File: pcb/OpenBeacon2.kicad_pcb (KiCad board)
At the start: 4 copper layers, 120 x 100 mm, 262 parts, among them J1 Bias V, J10 UART, J11 BNC, J12 USB_C_Receptacle, J13 UPDI, J14 PPS, J15 U.FL, J16 SMA CLKIN, J2 PAI+, J3 PAI-, J4 Digital IO, J5 ADC Inputs, J6 SMA, J8 I2C Bus, J9 GND, K1 G6K-2F-Y-DC5, K2 G6K-2F-Y-DC5, K3 G6K-2F-Y-DC5, K4 G6K-2F-Y-DC5, K5 G6K-2F-Y-DC5, K6 G6K-2F-Y-DC5, Q1 2N7002, Q2 MMBT4403, Q3 BS170, Q4 2N7002, Q5 2N7002, Q6 AO3400A, Q7 AO3400A, Q8 BS170, U1 TLV61046A, U10 CP2102N-A02-GQFN24, U11 TLV75533PDBV, U12 MAX-M10S-00B, U13 TPS22941, U2 25.000 MHz TCXO, U3 SN74LVC1G17, U4 SI5351C-B-GMR, U5 MCP4725A1T-E/CH, U8 24AA64T, U9 AVR128DA48-E/PT, Y1 32.768kHz

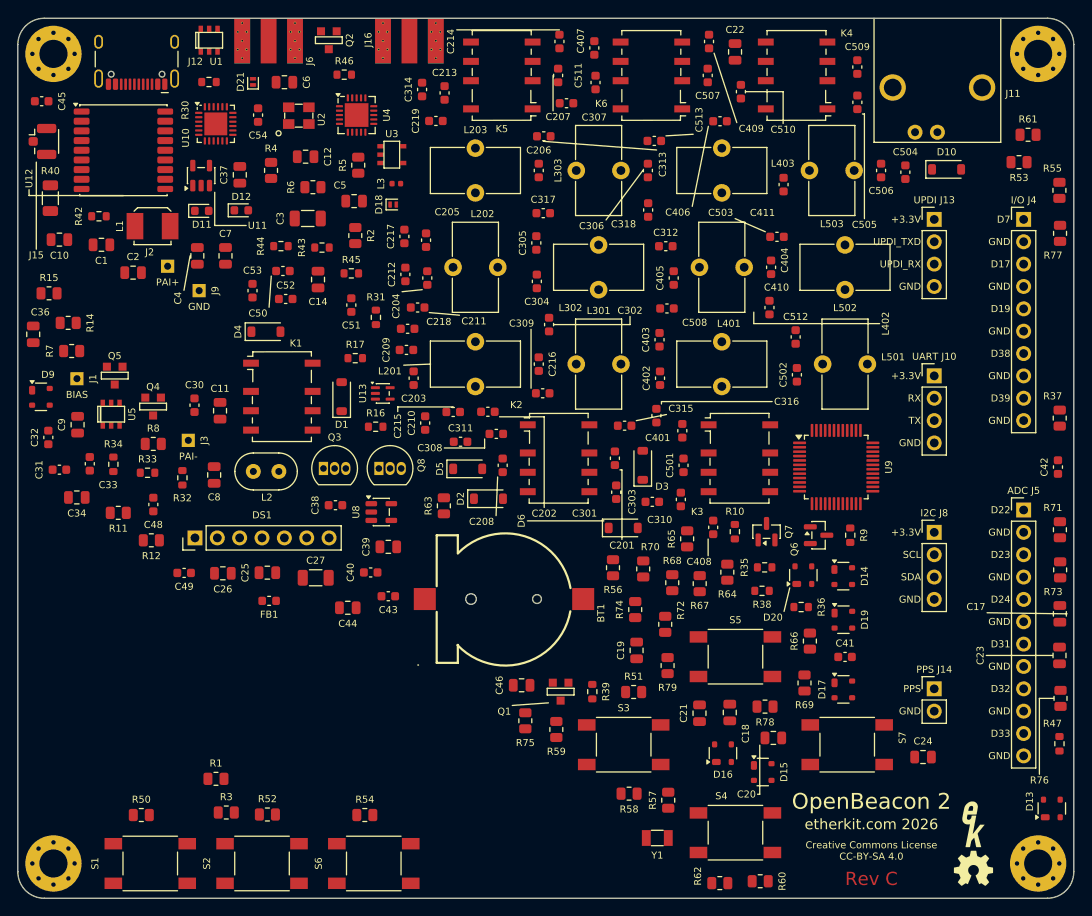
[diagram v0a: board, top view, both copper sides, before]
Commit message: S1-S7: Kinghelm KH-6X6X13H-STM 13 mm (C2837539); K5/K6 clear of case-bulkhead strip; gate check 7
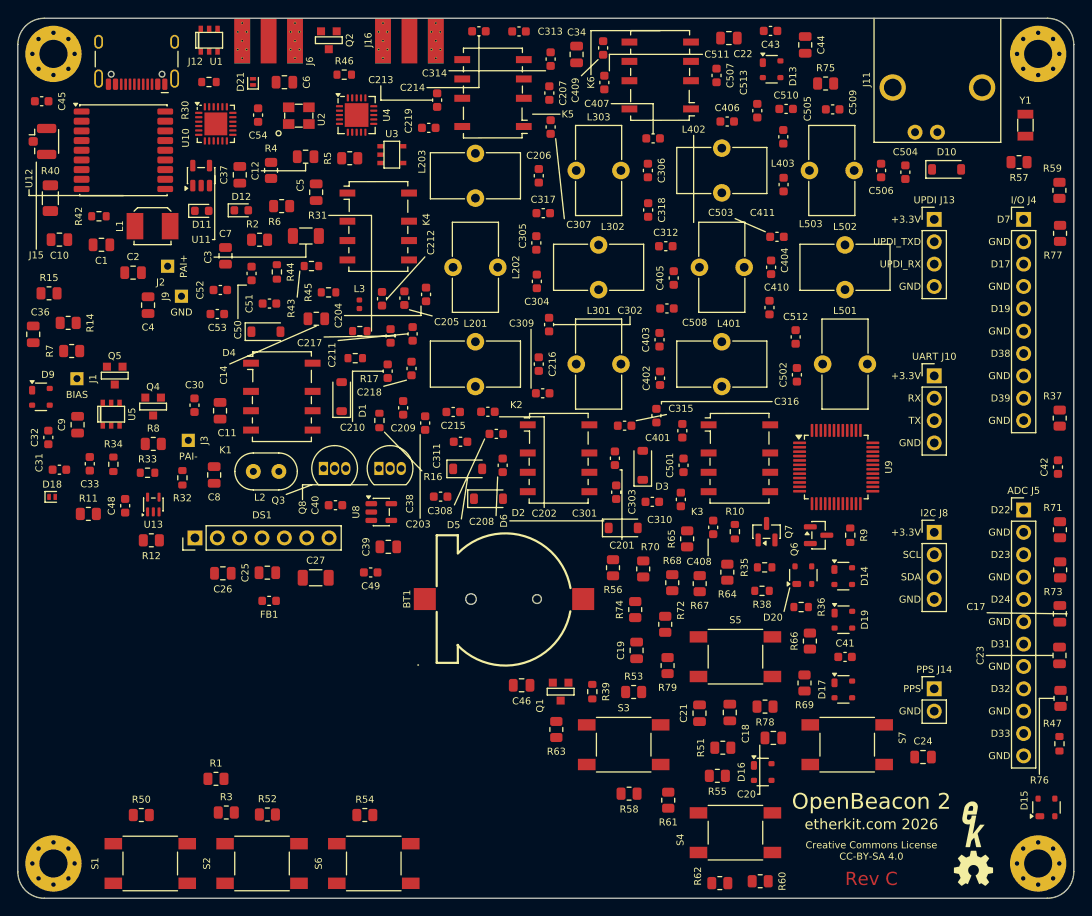
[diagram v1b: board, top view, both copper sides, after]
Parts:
- moved Y1 91.2 mm to (214.5, 112.2), turned to 90 degrees
- moved D13 89.8 mm to (185.7, 105.8), turned to 0 degrees
- moved R61 86.0 mm to (173.9, 188.9), turned to 90 degrees
- moved R59 83.8 mm to (218.4, 119.6)
- moved R57 82.7 mm to (213.8, 116.4), turned to 0 degrees
- moved C44 82.4 mm to (189.5, 103.0), turned to 90 degrees
- moved R75 80.1 mm to (191.8, 107.4), turned to 0 degrees
- moved C43 77.5 mm to (185.5, 101.4)
- moved R55 77.1 mm to (179.5, 186.1), turned to 0 degrees
- moved C34 75.9 mm to (163.5, 104.1), turned to 90 degrees
- moved R53 74.5 mm to (170.0, 176.6)
- moved D18 51.0 mm to (103.9, 154.4)
- moved K4 50.5 mm to (141.0, 123.7), turned to 0 degrees
- moved D15 32.5 mm to (216.9, 189.7), turned to 90 degrees
- moved U13 29.0 mm to (115.4, 155.3), turned to 90 degrees
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
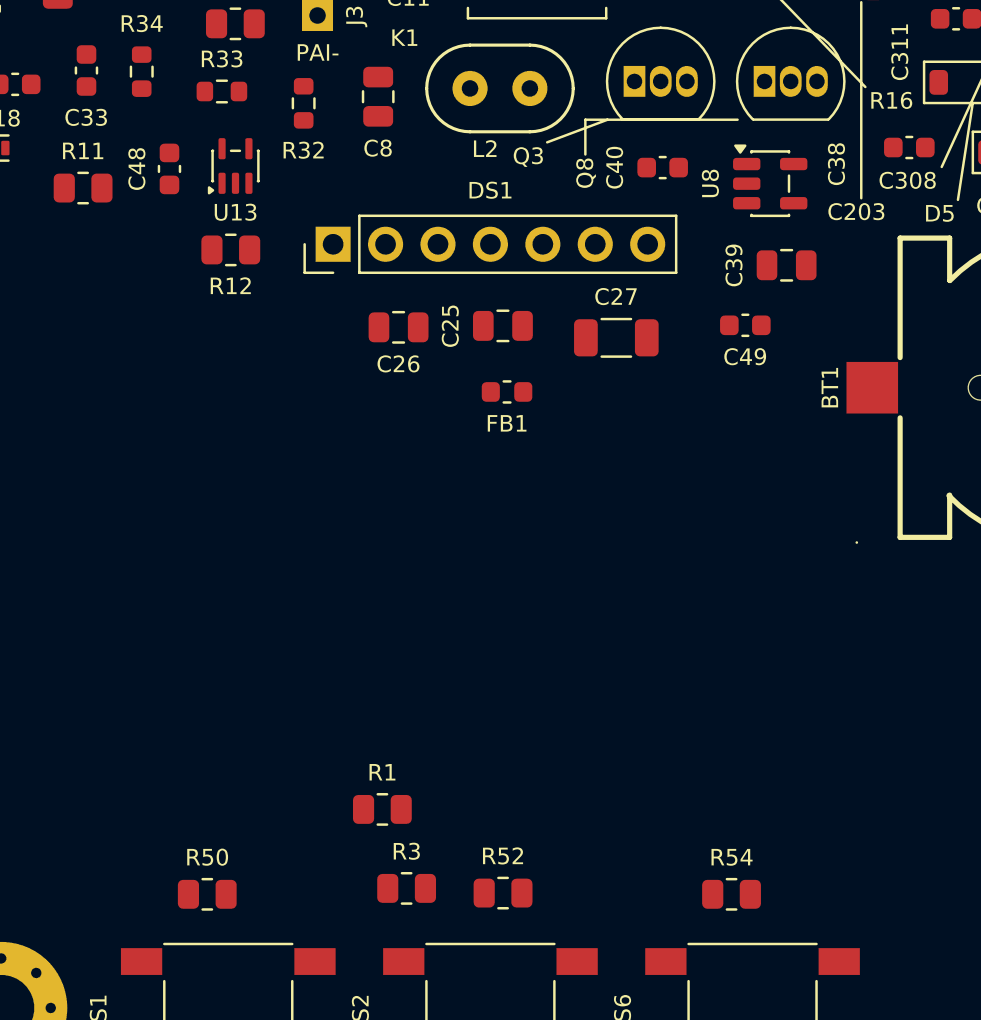
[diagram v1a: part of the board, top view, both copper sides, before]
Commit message: DS1: full 1.3in OLED module outline on F.SilkS (35.4x33.5, VFO style); U8 out from under module; gate check 8 (only low R/C/FB/L under DS1)
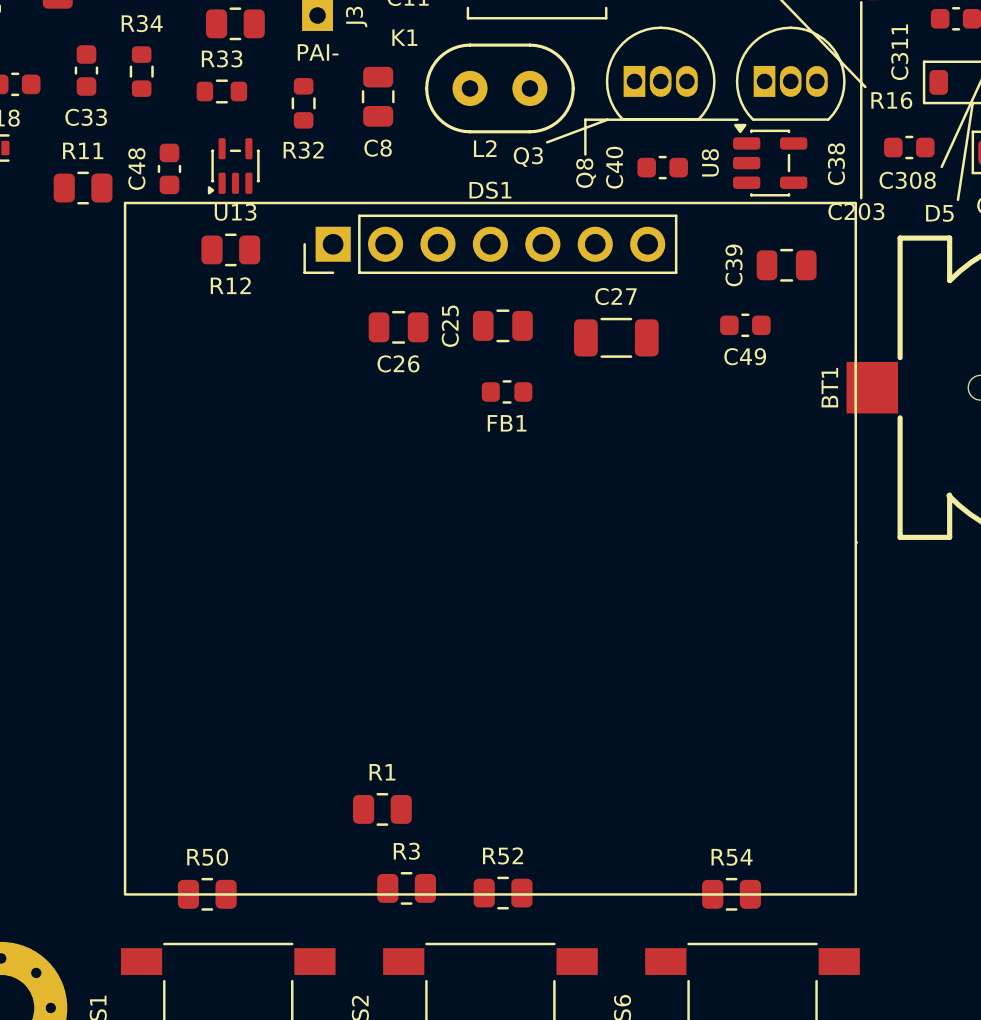
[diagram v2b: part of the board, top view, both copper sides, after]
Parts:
- moved U8 1.00 mm to (141.3, 155.1)
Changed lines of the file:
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@@
 		)
 		(fp_rect
+			(start 1.999999 -10.08)
+			(end -31.5 25.32)
+			(stroke
+				(width 0.12)
+				(type default)
+			)
+			(fill no)
+			(layer "F.SilkS")
+		)
+		(fp_rect
 			(start -1.77 -1.78)
 			(end 1.77 17.02)
@@
 	(footprint "Package_TO_SOT_SMD:SOT-23-5"
 		(layer "F.Cu")
-		(at 141.306103 156.112811)
+		(at 141.305 155.115)
 		(descr "SOT, 5 Pin (JEDEC MO-178 Var AA https://www.jedec.org/document_search?search_api_views_fulltext=MO-178)")
 		(tags "SOT TO_SOT_SMD")

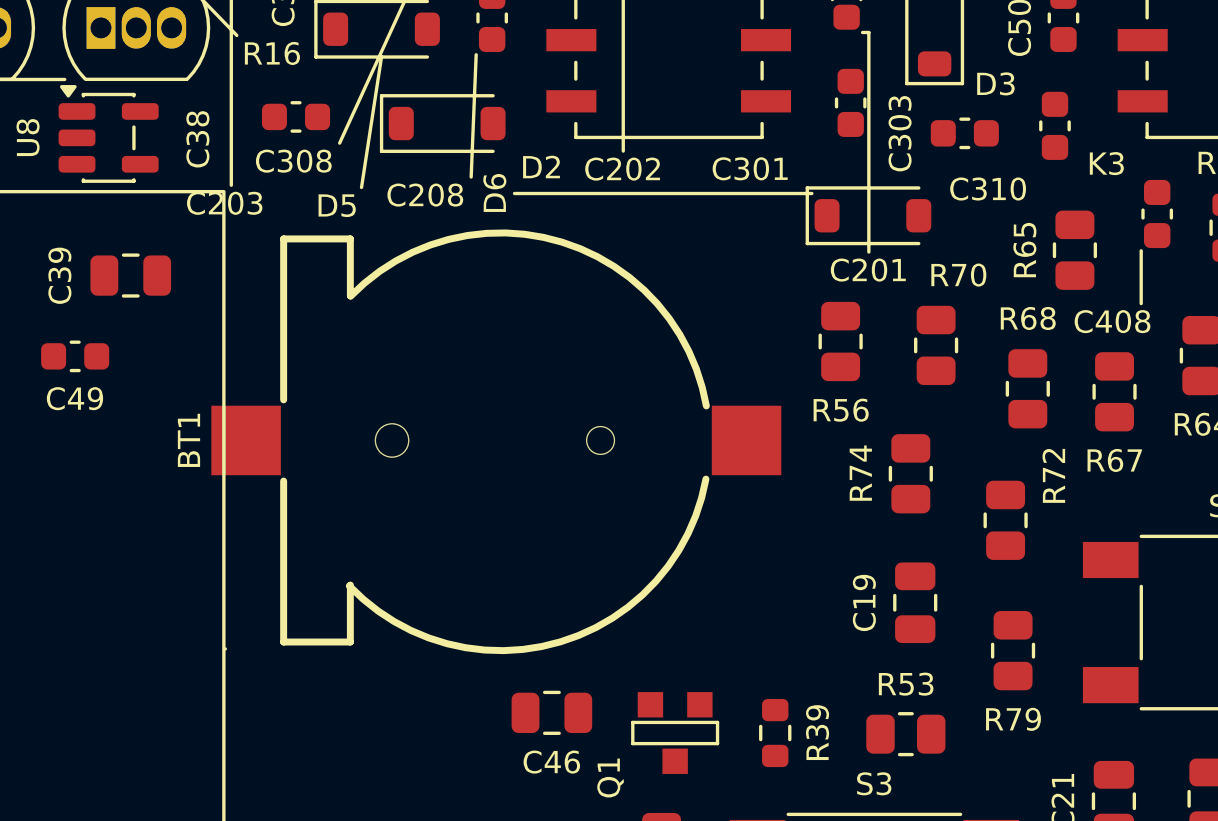
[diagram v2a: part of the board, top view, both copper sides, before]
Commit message: BT1 1.46 mm right: + pad was 0.45 mm inside the DS1 module outline, now 1.01 mm clear (D6/R56 nudged, C310 label); gate check 8 uses pads+courtyard and requires BT1 >= 1 mm
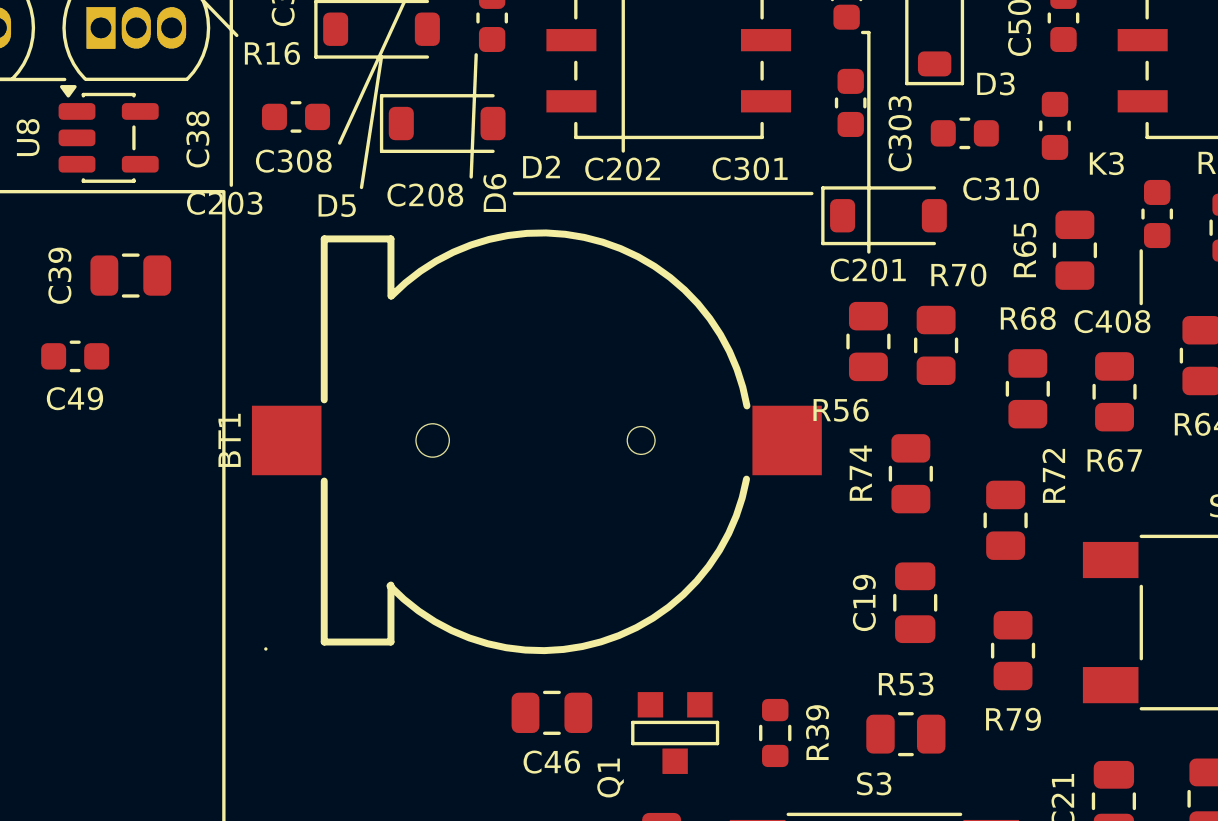
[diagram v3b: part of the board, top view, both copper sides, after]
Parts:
- moved BT1 1.46 mm to (156.7, 166.0)
- moved R56 1.00 mm to (168.6, 162.4)
- moved D6 0.56 mm to (169.4, 157.9)
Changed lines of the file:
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@@
 		(tags "capacitor")
 		(property "Reference" "C310"
-			(at -2.3 -2.4 0)
+			(at -2.3 -1.93006 0)
 			(layer "F.SilkS")
 			(effects
@@
 	(footprint "OB2:BAT-SMD_KH-CR1220-2"
 		(layer "F.Cu")
-		(at 155.25 166)
+		(at 156.71 166)
 		(property "Reference" "BT1"
 			(at -11.025 0 90)
@@
 	(footprint "Diode_SMD:D_SOD-123"
 		(layer "F.Cu")
-		(at 168.795865 157.91696)
+		(at 169.355865 157.91696)
 		(descr "SOD-123")
 		(tags "SOD-123")
 		(property "Reference" "D6"
-			(at -13.57 -0.8 90)
+			(at -14.13 -0.8 90)
 			(layer "F.SilkS")
 			(effects
@@
 		)
 		(fp_rect
-			(start 1.999999 -10.08)
+			(start 2 -10.08)
 			(end -31.5 25.32)
 			(stroke
@@
 	(footprint "Resistor_SMD:R_0805_2012Metric"
 		(layer "F.Cu")
-		(at 167.634907 162.440093 90)
+		(at 168.634907 162.440093 90)
 		(descr "Resistor SMD 0805 (2012 Metric), square (rectangular) end terminal, IPC-7351 nominal, (Body size source: IPC-SM-782 page 72, https://www.pcb-3d.com/wordpress/wp-content/uploads/ipc-sm-782a_amendment_1_and_2.pdf)")
 		(tags "resistor")
 		(property "Reference" "R56"
-			(at -2.5 0 0)
+			(at -2.5 -1 0)
 			(layer "F.SilkS")
 			(effects

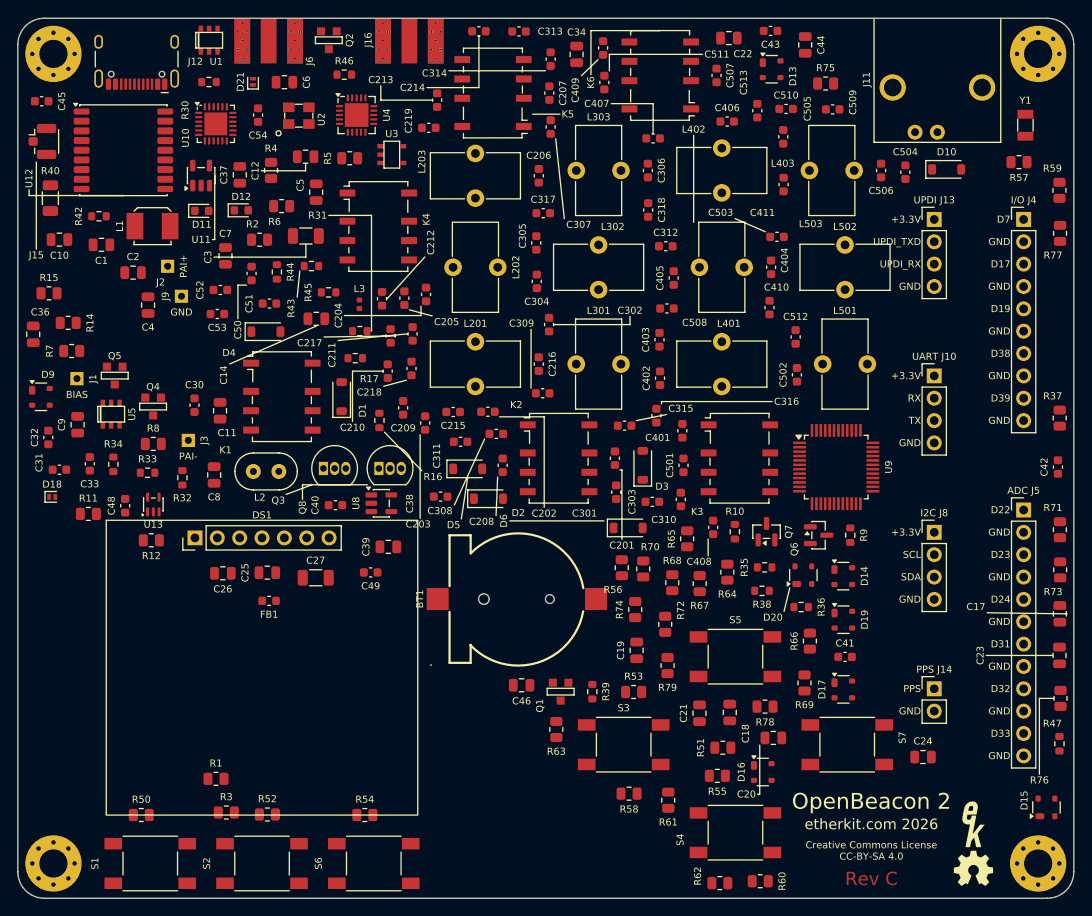
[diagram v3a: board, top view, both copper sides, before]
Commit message: GPS_TXD moved to U9 PF5 (pin 39, USART2 RXD ALT1): sch - PB1 NC, R68/HDR_D39 removed, J4.9/D14.3 NC; PCB - GPS_TXD 84 mm west part + new 75 mm east run, torn-up header/LED nets rerouted, HDR_D23 hand-routed, 3 clearance fixes, DRC 0/0; pro netclasses + .NetName DRU + SDA 0.15 mm rule
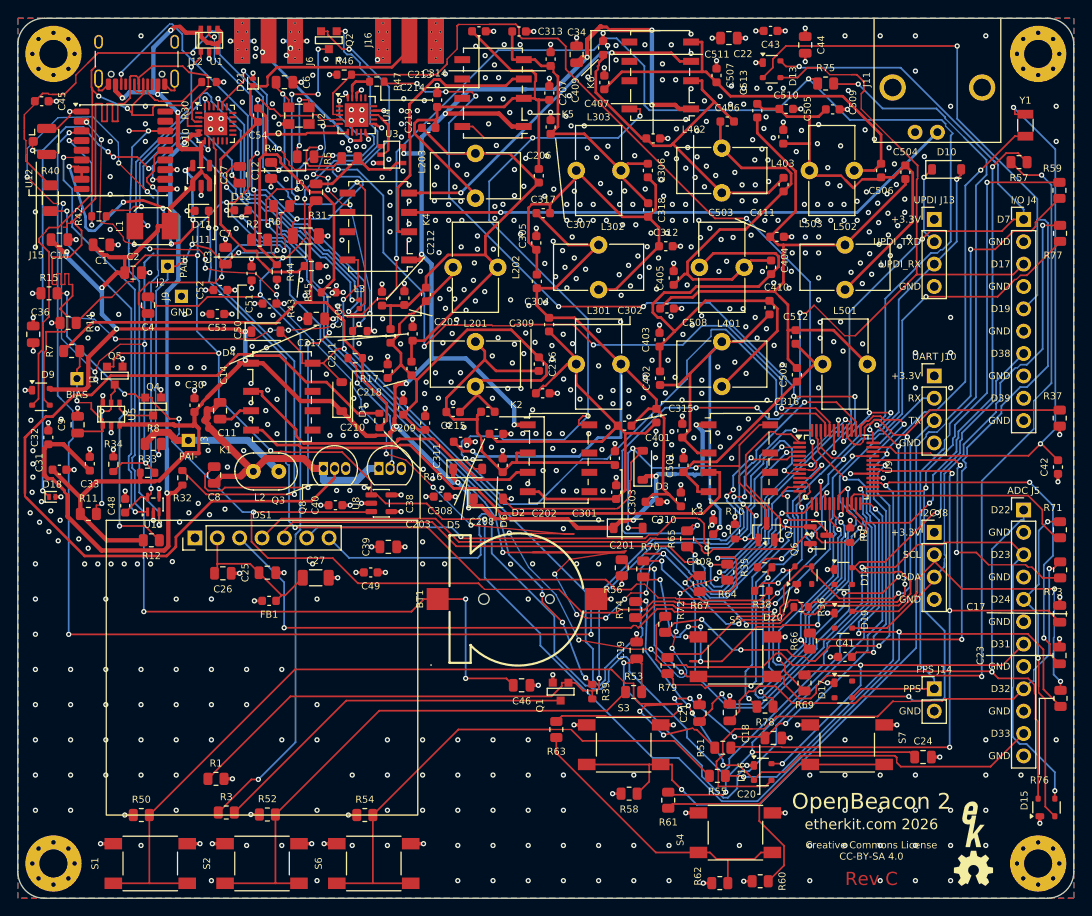
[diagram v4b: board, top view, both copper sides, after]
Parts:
- removed R68: 220R, Resistor_SMD:R_0805_2012Metric
- moved R47 108.1 mm to (140.8, 107.2), turned to 0 degrees
- turned K4 to 180 degrees
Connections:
- D14 pad 3: /I/O + UI/HDR_D39 -> unconnected-(D14-K-Pad3)
- J4 pad 9: /I/O + UI/HDR_D39 -> unconnected-(J4-Pin_9-Pad9)
- U9 pad 39: D39_A21_PF5 -> GPS_TXD
- U9 pad 5: GPS_TXD -> unconnected-(U9-PB1-Pad5)
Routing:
- net +5V: track 0.00 -> 354.5 mm, vias 0 -> 23
- net SDA: track 0.00 -> 250.3 mm, vias 0 -> 18
- net SCL: track 0.00 -> 249.0 mm, vias 0 -> 10
- net GPS_PPS: track 0.00 -> 197.5 mm, vias 0 -> 5
- net GPS_TXD: track 0.00 -> 160.2 mm, vias 0 -> 18
- net GPS_RXD: track 0.00 -> 159.0 mm, vias 0 -> 6
- net /Filter Bank/COIL_B: track 0.00 -> 155.0 mm, vias 0 -> 8
- net GND: track 0.00 -> 153.7 mm, vias 0 -> 729
- net Net-(C37-Pad2): track 0.00 -> 136.0 mm, vias 0 -> 10
- net /I/O + UI/HDR_D19: track 0.00 -> 129.4 mm, vias 0 -> 2
- net Net-(Q2-B): track 0.00 -> 122.6 mm, vias 0 -> 5
- net /Filter Bank/COIL_A: track 0.00 -> 121.9 mm, vias 0 -> 3
- net Net-(R56-Pad2): track 0.00 -> 119.6 mm, vias 0 -> 4
- net /I/O + UI/HDR_D17: track 0.00 -> 118.8 mm, vias 0 -> 4
- net /MCU + USB/MCU_RX: track 0.00 -> 116.8 mm, vias 0 -> 2
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- added copper zone on In2.Cu, net +3.3V
- added copper zone on B.Cu, net GND
- added copper zone on F.Cu, net GND
- added copper zone on In1.Cu, net GND
- added copper zone on In2.Cu, net GND
